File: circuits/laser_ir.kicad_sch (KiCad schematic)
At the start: 11 parts, among them Q1 AO3400A, U5 TLV9001

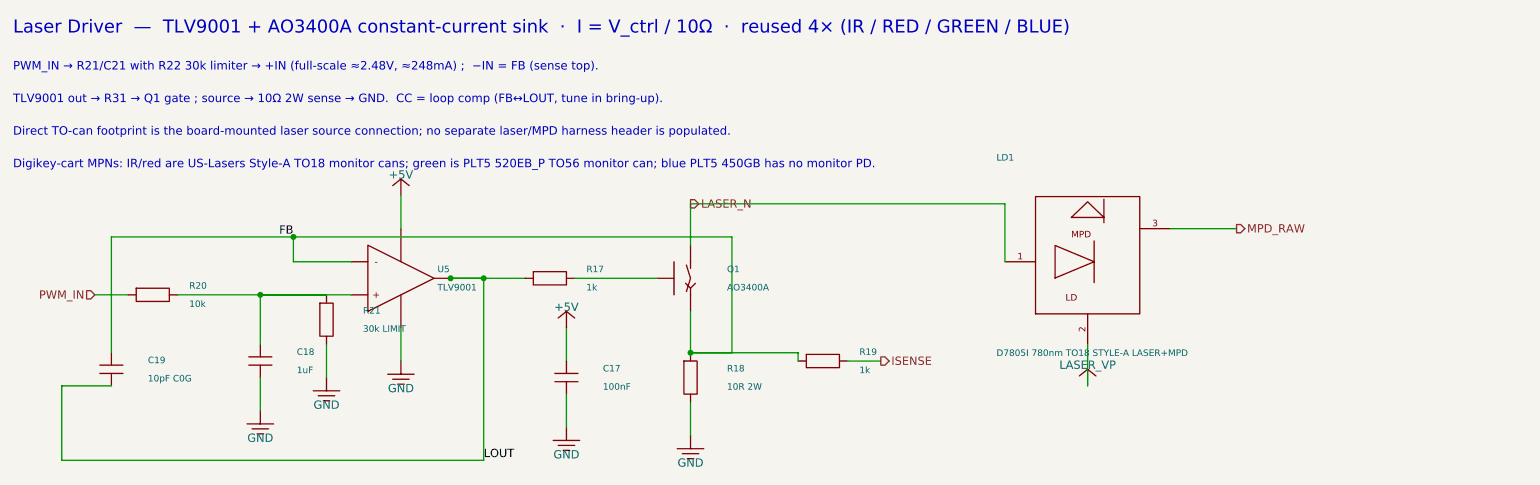
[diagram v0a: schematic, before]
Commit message: Limit laser command current per channel
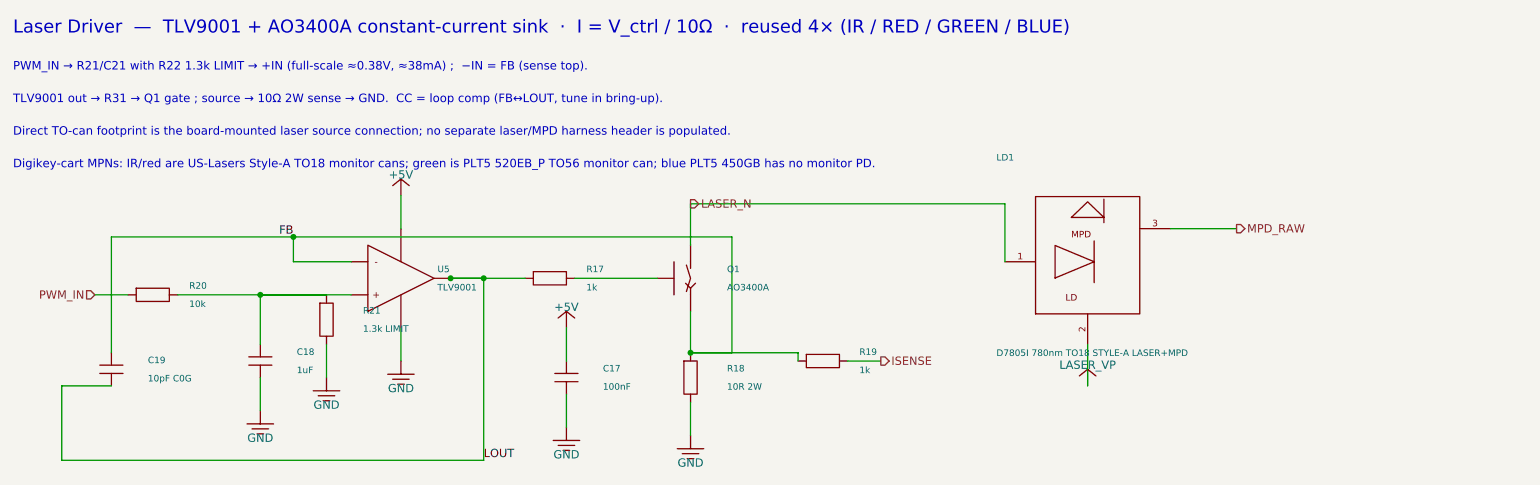
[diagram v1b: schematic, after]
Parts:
- R21: value 30k LIMIT -> 1.3k LIMIT; LCSC C22984 -> C22767; Part Number 0603WAF3002T5E -> 0603WAF1301T5E
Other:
- note added: "PWM_IN → R21/C21 with R22 1.3k LIMIT → +IN (full-scale ≈0.38V, ≈38mA) ; −IN = FB (sense top)."
- note removed: "PWM_IN → R21/C21 with R22 30k limiter → +IN (full-scale ≈2.48V, ≈248mA) ; −IN = FB (sense top)."
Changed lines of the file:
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@@
     (in_bom yes) (on_board yes) (dnp no)
     (property "Reference" "R21" (at 203.72 157.35 0) (effects (font (size 1.0 1.0)) (justify left)))
-    (property "Value" "30k LIMIT" (at 203.72 160.15 0) (effects (font (size 1.0 1.0)) (justify left)))
+    (property "Value" "1.3k LIMIT" (at 203.72 160.15 0) (effects (font (size 1.0 1.0)) (justify left)))
     (property "Footprint" "Resistor_SMD:R_0603_1608Metric_Pad0.98x0.95mm_HandSolder" (at 198.12 158.75 0) (effects (font (size 1.0 1.0)) hide))
     (property "Datasheet" "" (at 198.12 158.75 0) (effects (font (size 1.0 1.0)) hide))
-    (property "Part Number" "0603WAF3002T5E" (at 198.12 158.75 0) (effects (font (size 1.0 1.0)) hide))
-    (property "LCSC" "C22984" (at 198.12 158.75 0) (effects (font (size 1.0 1.0)) hide))
+    (property "Part Number" "0603WAF1301T5E" (at 198.12 158.75 0) (effects (font (size 1.0 1.0)) hide))
+    (property "LCSC" "C22767" (at 198.12 158.75 0) (effects (font (size 1.0 1.0)) hide))
     (pin "1")
     (pin "2")
@@
   (label "LOUT" (at 222.25 180.34 0) (effects (font (size 1.27 1.27)) (justify left bottom)))
   (text "Laser Driver  —  TLV9001 + AO3400A constant-current sink  ·  I = V_ctrl / 10Ω  ·  reused 4× (IR / RED / GREEN / BLUE)" (at 150 114 0) (effects (font (size 2.0 2.0)) (justify left)))
-  (text "PWM_IN → R21/C21 with R22 30k limiter → +IN (full-scale ≈2.48V, ≈248mA) ;  −IN = FB (sense top)." (at 150 120 0) (effects (font (size 1.3 1.3)) (justify left)))
+  (text "PWM_IN → R21/C21 with R22 1.3k LIMIT → +IN (full-scale ≈0.38V, ≈38mA) ;  −IN = FB (sense top)." (at 150 120 0) (effects (font (size 1.3 1.3)) (justify left)))
   (text "TLV9001 out → R31 → Q1 gate ; source → 10Ω 2W sense → GND.  CC = loop comp (FB↔LOUT, tune in bring-up)." (at 150 125 0) (effects (font (size 1.3 1.3)) (justify left)))
   (text "Direct TO-can footprint is the board-mounted laser source connection; no separate laser/MPD harness header is populated." (at 150 130 0) (effects (font (size 1.3 1.3)) (justify left)))

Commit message: Checkpoint laser controller fab parity package
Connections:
- net CMD_FILTER: now reaches C18.1, R20.2, R21.1, U5.3 (+)
- net GATE: now reaches Q1.1 (G), R17.2
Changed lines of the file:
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@@
   (junction (at 193.04 146.05) (diameter 0) (color 0 0 0 0))
   (junction (at 222.25 152.4) (diameter 0) (color 0 0 0 0))
+  (label "CMD_FILTER" (at 187.96 154.94 0) (effects (font (size 1.27 1.27)) (justify left bottom)))
+  (label "LOUT" (at 228.6 152.4 0) (effects (font (size 1.27 1.27)) (justify left bottom)))
+  (label "GATE" (at 248.92 152.4 0) (effects (font (size 1.27 1.27)) (justify left bottom)))
   (hierarchical_label "PWM_IN" (shape input) (at 162.56 154.94 0) (effects (font (size 1.27 1.27)) (justify right)))
   (hierarchical_label "ISENSE" (shape output) (at 283.21 165.1 0) (effects (font (size 1.27 1.27)) (justify left)))

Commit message: Checkpoint schematic warning hygiene
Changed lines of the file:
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@@
   (wire (pts (xy 187.96 167.64) (xy 187.96 172.72)) (stroke (width 0) (type default)))
   (wire (pts (xy 198.12 162.56) (xy 198.12 167.64)) (stroke (width 0) (type default)))
-  (wire (pts (xy 217.17 152.4) (xy 228.6 152.4)) (stroke (width 0) (type default)))
-  (wire (pts (xy 236.22 152.4) (xy 248.92 152.4)) (stroke (width 0) (type default)))
+  (wire (pts (xy 217.17 152.4) (xy 223.52 152.4)) (stroke (width 0) (type default)))
+  (wire (pts (xy 223.52 152.4) (xy 228.6 152.4)) (stroke (width 0) (type default)))
+  (wire (pts (xy 236.22 152.4) (xy 242.57 152.4)) (stroke (width 0) (type default)))
+  (wire (pts (xy 242.57 152.4) (xy 248.92 152.4)) (stroke (width 0) (type default)))
   (wire (pts (xy 254 157.48) (xy 254 163.83)) (stroke (width 0) (type default)))
   (wire (pts (xy 254 171.45) (xy 254 176.53)) (stroke (width 0) (type default)))
   (wire (pts (xy 254 163.83) (xy 270.51 163.83)) (stroke (width 0) (type default)))
   (wire (pts (xy 270.51 163.83) (xy 270.51 165.1)) (stroke (width 0) (type default)))
+  (wire (pts (xy 223.52 152.4) (xy 223.52 144.78)) (stroke (width 0) (type default)))
+  (wire (pts (xy 242.57 152.4) (xy 242.57 144.78)) (stroke (width 0) (type default)))
   (wire (pts (xy 167.64 154.94) (xy 162.56 154.94)) (stroke (width 0) (type default)))
   (wire (pts (xy 278.13 165.1) (xy 283.21 165.1)) (stroke (width 0) (type default)))
@@
   (junction (at 254 163.83) (diameter 0) (color 0 0 0 0))
   (junction (at 217.17 152.4) (diameter 0) (color 0 0 0 0))
+  (junction (at 223.52 152.4) (diameter 0) (color 0 0 0 0))
+  (junction (at 242.57 152.4) (diameter 0) (color 0 0 0 0))
   (junction (at 193.04 146.05) (diameter 0) (color 0 0 0 0))
   (junction (at 222.25 152.4) (diameter 0) (color 0 0 0 0))
   (label "CMD_FILTER" (at 187.96 154.94 0) (effects (font (size 1.27 1.27)) (justify left bottom)))
-  (label "LOUT" (at 228.6 152.4 0) (effects (font (size 1.27 1.27)) (justify left bottom)))
-  (label "GATE" (at 248.92 152.4 0) (effects (font (size 1.27 1.27)) (justify left bottom)))
+  (label "LOUT" (at 223.52 144.78 0) (effects (font (size 1.27 1.27)) (justify left bottom)))
+  (label "GATE" (at 242.57 144.78 0) (effects (font (size 1.27 1.27)) (justify left bottom)))
   (hierarchical_label "PWM_IN" (shape input) (at 162.56 154.94 0) (effects (font (size 1.27 1.27)) (justify right)))
   (hierarchical_label "ISENSE" (shape output) (at 283.21 165.1 0) (effects (font (size 1.27 1.27)) (justify left)))
